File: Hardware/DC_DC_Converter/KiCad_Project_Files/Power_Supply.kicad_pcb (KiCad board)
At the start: 2 copper layers, 100 x 50 mm, 106 parts, among them J2 Conn_01x01, J3 Conn_01x01, J4 Screw_Terminal_01x02, J5 USB_C_Receptacle_USB2.0, Q1 FDN335N, Q2 FDN335N, Q3 FDN335N, SW1 UP, SW2 DW, SW3 V_I_SEL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

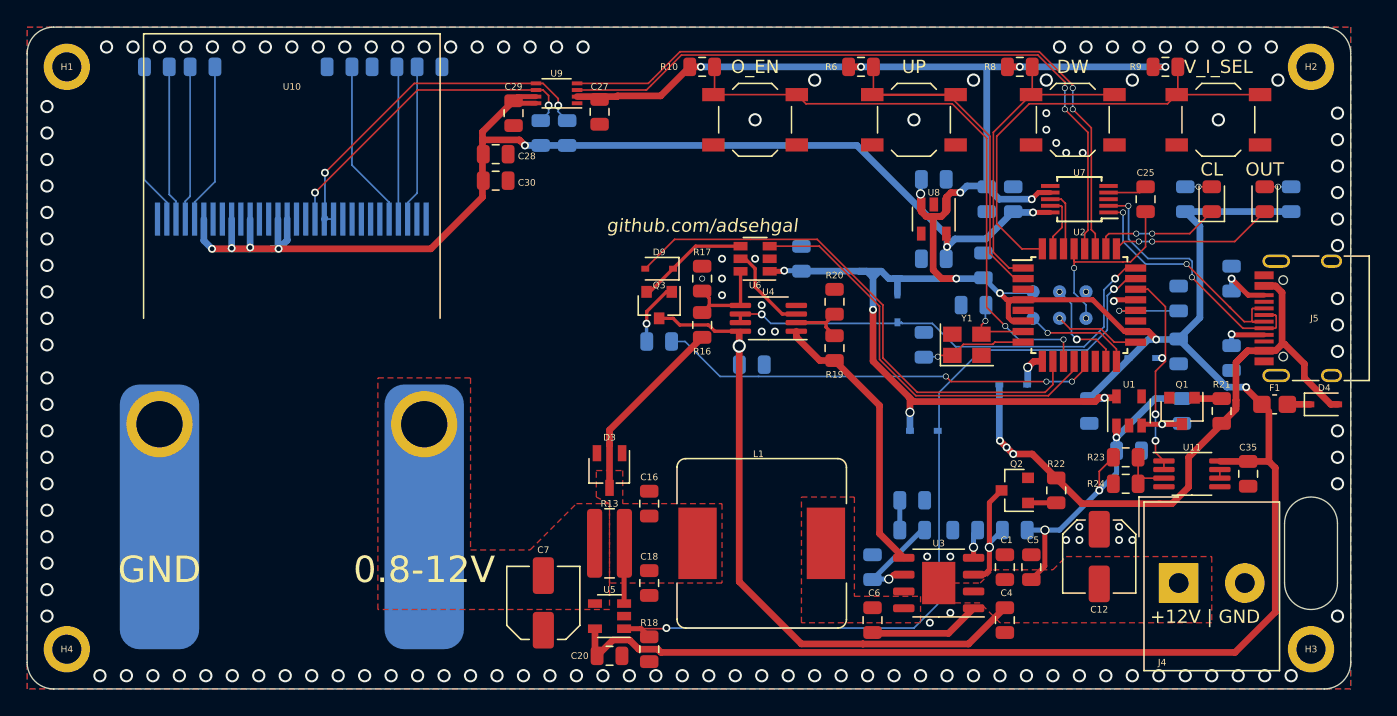
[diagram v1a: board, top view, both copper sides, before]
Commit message: fixed buffer errors
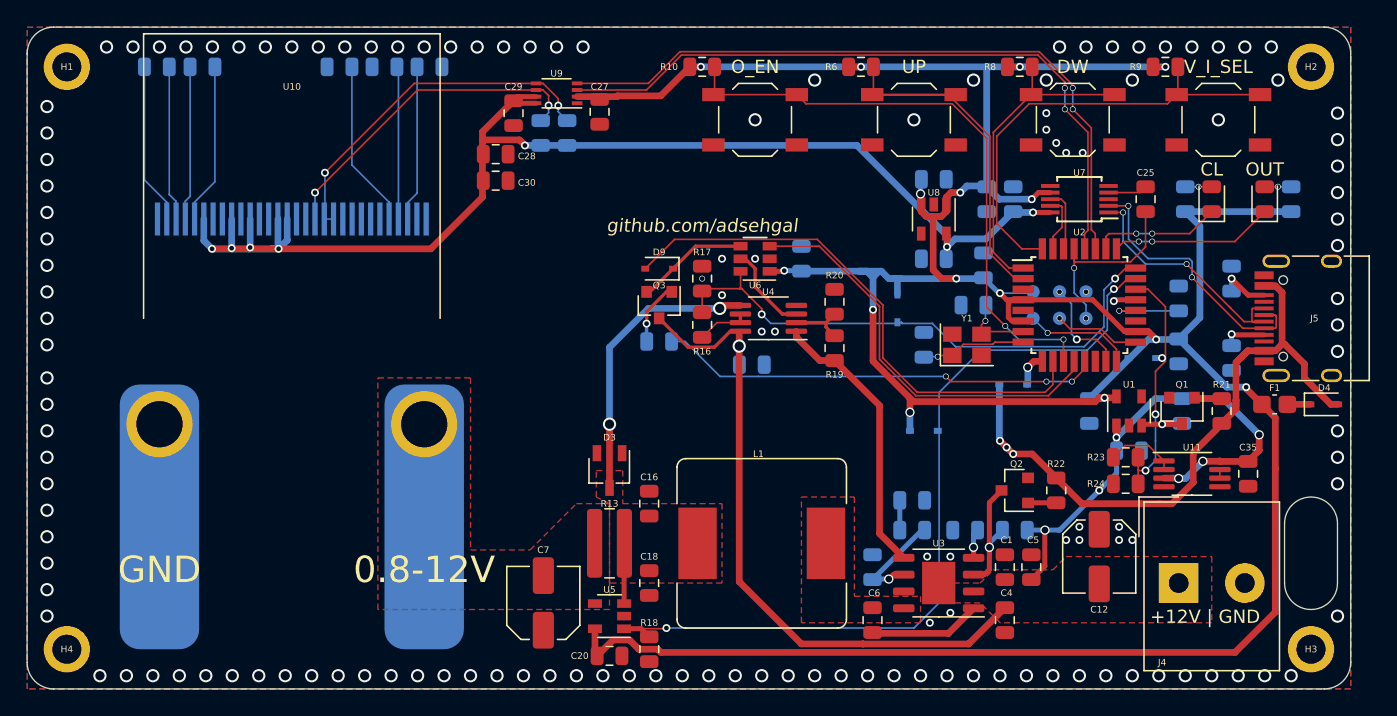
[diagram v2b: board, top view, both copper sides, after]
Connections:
- C35 pad 2: +5V -> +VSW
- R16 pad 1: Net-(R16-Pad1) -> /V_SENSE
- R16 pad 2: Net-(C16-Pad2) -> Net-(R16-Pad2)
- R17 pad 2: Net-(R16-Pad1) -> /V_SENSE
- R23 pad 1: +VSW -> /Vin
- R23 pad 2: /Vin -> Net-(D8-Pad2)
- R24 pad 2: /Vin -> Net-(D8-Pad2)
- U11 pad 1: Net-(D8-Pad2) -> /Vin
- U11 pad 2: Net-(D8-Pad2) -> /Vin
- U11 pad 3: /Vin -> +VSW
- U11 pad 8: +5V -> +VSW
- U4 pad 5: Net-(R16-Pad1) -> Net-(C16-Pad2)
- U4 pad 6: /V_SENSE -> Net-(R16-Pad2)
- U4 pad 7: /V_SENSE -> Net-(R16-Pad2)
- U6 pad 6: Net-(R16-Pad1) -> /V_SENSE
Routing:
- net +VSW: track 75.5 -> 89.8 mm, vias 4 -> 7
- net Net-(C16-Pad2): track 18.8 -> 26.3 mm, vias 0 -> 2
- net Net-(R16-Pad1): track 7.00 -> 0.00 mm
- net /V_SENSE: track 35.8 -> 41.9 mm
- net +5V: track 270.3 -> 265.7 mm
- net Net-(R16-Pad2): track 0.00 -> 4.00 mm
- net Net-(D8-Pad2): track 16.4 -> 19.1 mm
- net /Vin: track 4.13 -> 5.33 mm
- net /I_SENSE: track 62.8 -> 62.0 mm
- net /SW1: track 30.8 -> 30.0 mm
- net /POT_U~D: track 31.5 -> 30.8 mm
- net /POT_VIHH: track 33.4 -> 32.9 mm
- net GND: vias 140 -> 138
